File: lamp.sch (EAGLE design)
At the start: 60 parts, among them P1 10kΩ

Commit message: Finished footprint for header block. Fiddled around switch and brightness circuits. Fine-tuned placements of several parts. Added labels for switch/brightness adjustment trimpots. I think this is pretty much done.
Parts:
- removed R13: (no value), Barebones-Arduino:RESISTOR-SMD
- removed U$31: CLA1BWKWMKW-4, lamp:CLA1BWKWMKW-4
- added C4: 100pF, Barebones-Arduino:CAPACITOR-SMD
- added P2: 2MΩ, lamp:PVG3G
- added U$19: CLA1BWKWMKW-4, lamp:CLA1BWKWMKW-4
- R11: value 1MΩ -> (none)
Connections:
- removed net N$12 (its old number): U$12.P$4, U$13.P$2
- removed net N$21 (its old number): U$21.P$4, U$22.P$2
- removed net N$24 (its old number): U$24.P$4, U$25.P$2
- removed net N$27 (its old number): U$27.P$4, U$28.P$2
- removed net N$3 (its old number): U$3.P$4, U$4.P$2
- removed net N$30 (its old number): U$30.P$4, U$31.P$2
- removed net N$6 (its old number): U$6.P$4, U$7.P$2
- removed net N$9 (its old number): U$10.P$2, U$9.P$4
- new net N$1: U$1.P$4, U$2.P$2
- new net N$10: U$10.P$4, U$11.P$2
- new net N$19: U$19.P$4, U$20.P$2
- new net N$22: U$22.P$4, U$23.P$2
- new net N$25: U$25.P$4, U$26.P$2
- new net N$28: U$28.P$4, U$29.P$2
- new net N$4: U$4.P$4, U$5.P$2
- new net N$7: U$7.P$4, U$8.P$2
- net +5V: now also R11.2; no longer R12.2
- net GND: now also C4.2, R12.1; no longer R13.1
- net N$11: now also U$12.P$4; no longer U$13.P$4
- net N$15: now also C4.1, P2.P$3; no longer R11.2
- net N$17: now also R11.1; no longer R12.1
- net N$2: now also U$3.P$4; no longer U$4.P$4
- net N$20: now also U$21.P$4; no longer U$22.P$4
- net N$23: now also U$24.P$4; no longer U$25.P$4
- net N$26: now also U$27.P$4; no longer U$28.P$4
- net N$29: now also U$30.P$4; no longer U$31.P$4
- net N$31: now also U$13.P$4; no longer U$1.P$4
- net N$44: now also R12.2; no longer R13.2
- net N$45: now also U$10.P$2, U$13.P$2, U$19.P$2, U$22.P$2, U$25.P$2, U$28.P$2, U$4.P$2, U$7.P$2; no longer U$11.P$2, U$2.P$2, U$20.P$2, U$23.P$2, U$26.P$2, U$29.P$2, U$5.P$2, U$8.P$2
- net N$5: now also U$6.P$4; no longer U$7.P$4
- net N$51: now also P2.P$2; no longer R11.1
- net N$8: now also U$9.P$4; no longer U$10.P$4
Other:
- moved on the sheet: R11, R12

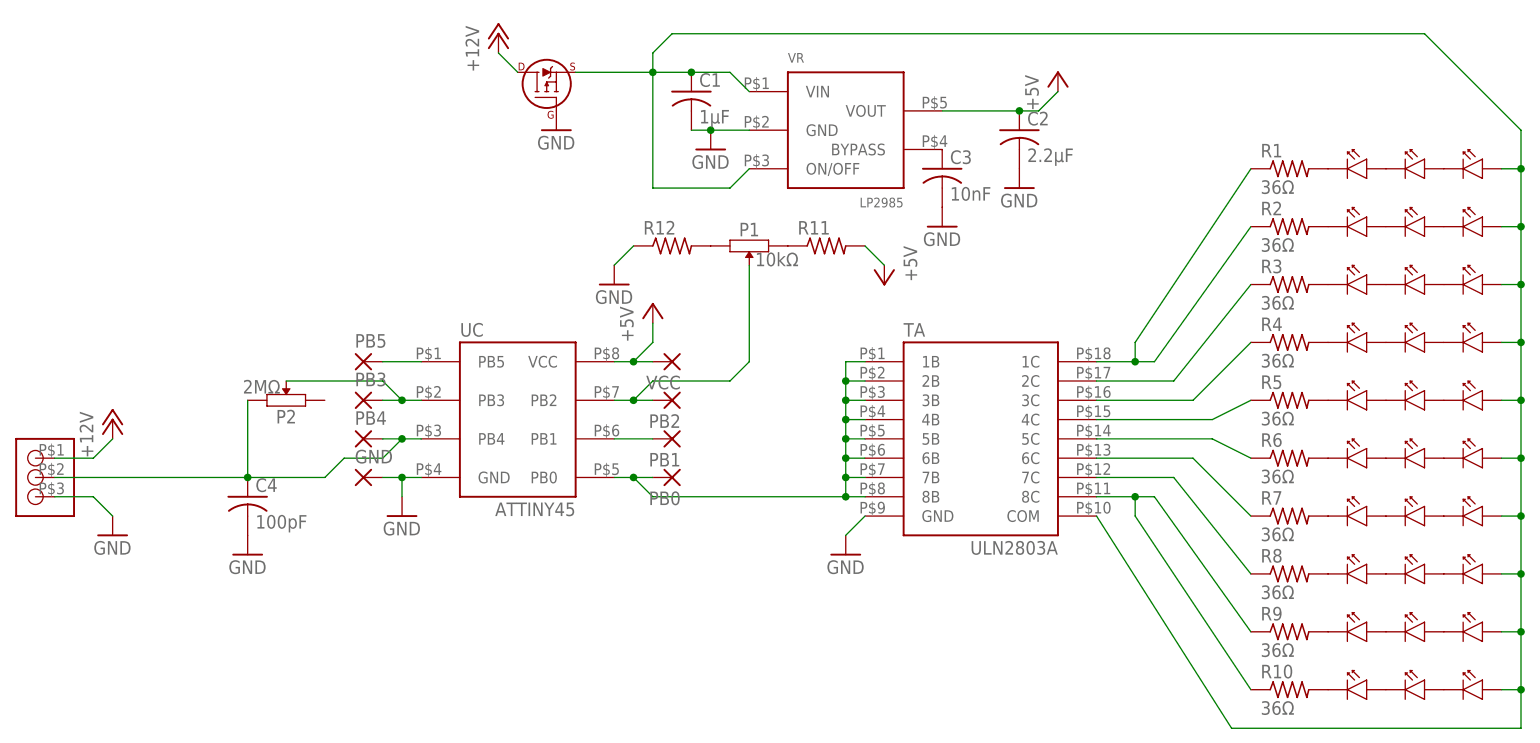
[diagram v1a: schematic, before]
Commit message: Fixed footprint for trimpots. Removed transistor array and replaced with single n fet. Adjusted layout for new/modified parts. Increased font size for all board markings. Changed capacitive switch pins on attiny45 for nicer layout. Shuffled ground plane vias.
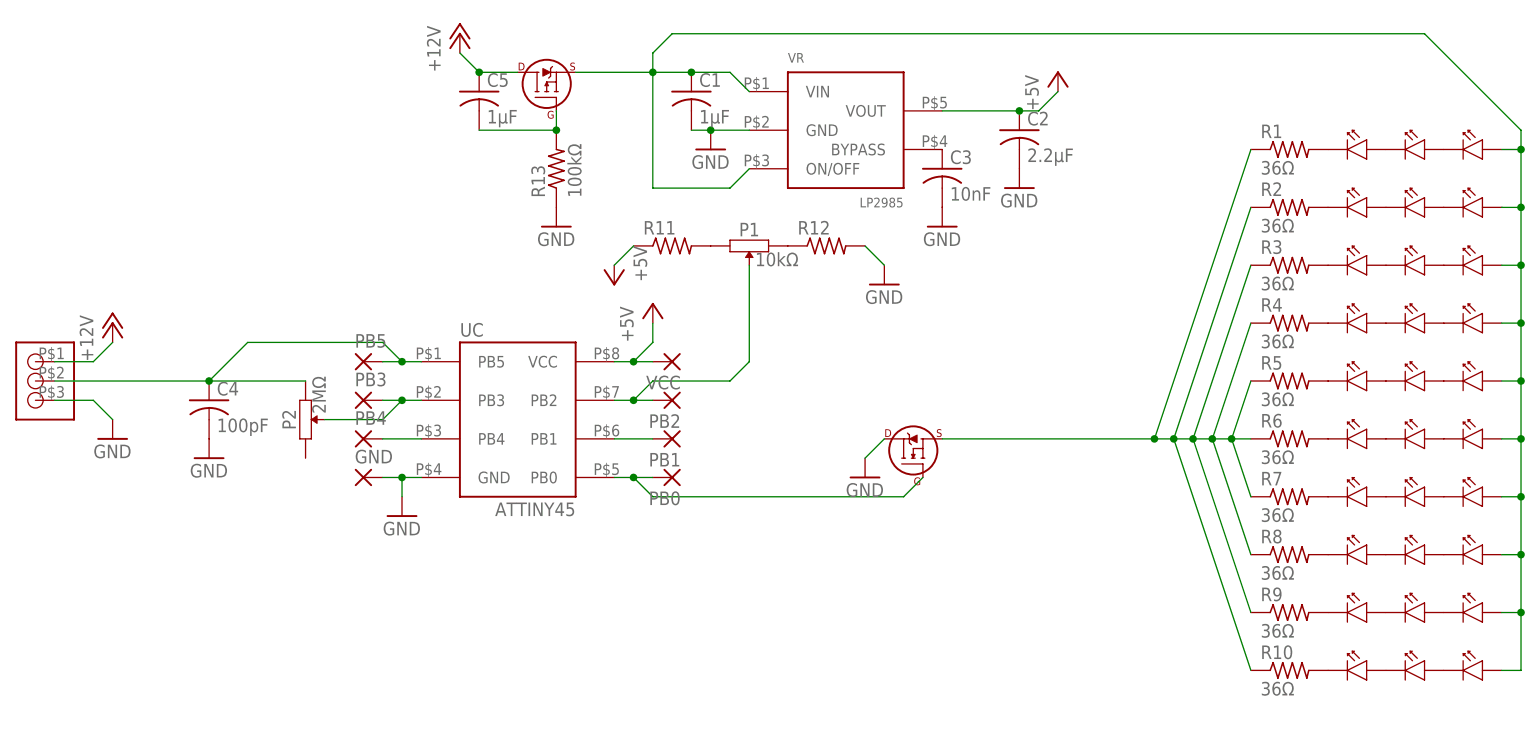
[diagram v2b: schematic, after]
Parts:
- removed TA: ULN2803A, lamp:ULN2803A
- added C5: 1µF, Barebones-Arduino:CAPACITOR-SMD
- added F2: SI2319DS, lamp:SI2319DS
- added R13: 100kΩ, Barebones-Arduino:RESISTOR-SMD
- F1: value SI2319DS -> SI2318DS; device lamp:SI2319DS -> lamp:SI2318DS
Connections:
- removed net N$15: C4.1, P2.P$3, PB4.P, U$32.P$2, UC.PB4
- removed net N$35: R10.1, R9.1, TA.8C
- removed net N$36 (its old number): R4.1, TA.3C
- removed net N$38: R1.1, R2.1, TA.1C
- removed net N$41: R6.1, TA.5C
- removed net N$42: R5.1, TA.4C
- removed net N$44: P1.P$1, R12.2
- removed net N$49: F1.DRAIN, U$32.P$1
- new net +12V: C5.1, F2.DRAIN, U$32.P$1
- new net N$14: C5.2, F2.GATE, R13.2
- net +5V: now also R11.1; no longer R11.2
- net GND: now also F1.DRAIN, R12.2, R13.1; no longer F1.GATE, R12.1, TA.GND
- net N$17: now also R11.2; no longer R11.1
- net N$18: now also C4.1, P2.P$1, U$32.P$2
- net N$33: now also F1.SOURCE, R1.1, R10.1, R2.1, R3.1, R4.1, R5.1, R6.1, R8.1, R9.1; no longer TA.6C
- net N$34: now also P1.P$1, R12.1; no longer R8.1, TA.7C
- net N$37: now also PB4.P, UC.PB4; no longer R3.1, TA.2C
- net N$45: now also F2.SOURCE; no longer F1.SOURCE, TA.COM
- net N$47: now also F1.GATE; no longer TA.1B, TA.2B, TA.3B, TA.4B, TA.5B, TA.6B, TA.7B, TA.8B
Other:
- moved on the sheet: C4, P2, R1, R10, R11, R12, R2, R3, R4, R5, R6, R7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
